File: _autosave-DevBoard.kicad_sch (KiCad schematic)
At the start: 135 parts, among them J1 Audio_In, J10 Jumper, J11 RJ45, J12 Jumper, J13 Jumper, J14 Jumper, J15 Jumper, J16 Jumper, J17 Jumper, J18 DAC_I2S, J19 DAC_OUT, J2 Audio_In, J20 DAC_Amplified, J21 DAC_Amplified, J22 Voltmeter_Power, J23 Voltmeter_Positive, J24 Voltmeter_Ground, J25 Conn_01x05_Pin, J26 Pot1, J27 Pot2, J28 Pot3, J29 Pot4, J3 Audio_Amplified, J30 CV_Scaled_Out1, J31 Audio12V_In, J32 Audio_Scaled_Out, J33 CV_In2, J34 Power, J35 Power, J36 Power, J37 Power, J38 Power, J39 Power_Test, J4 Audio_Amplified, J40 Power, J41 Power_Test, J42 Power, J43 Power, J44 Pot1, J45 Pot2, J46 Pot3, J47 Pot4, J48 CV_In1, J49 CV_Scaled_Out2, J5 CV_In, J50 Audio12V_In, J51 Audio_Scaled_Out, J6 CV_In, J7 CV_Amplified, J8 CV_Amplified, J9 Jumper, SW2 SW_DPDT_x2, U1 MCP6004, U2 TL074, U3 LM1117-3.3, U4 LM1117-5.0, U5 LM4040DBZ-5, U6 PCM5100APW, U8 TL072

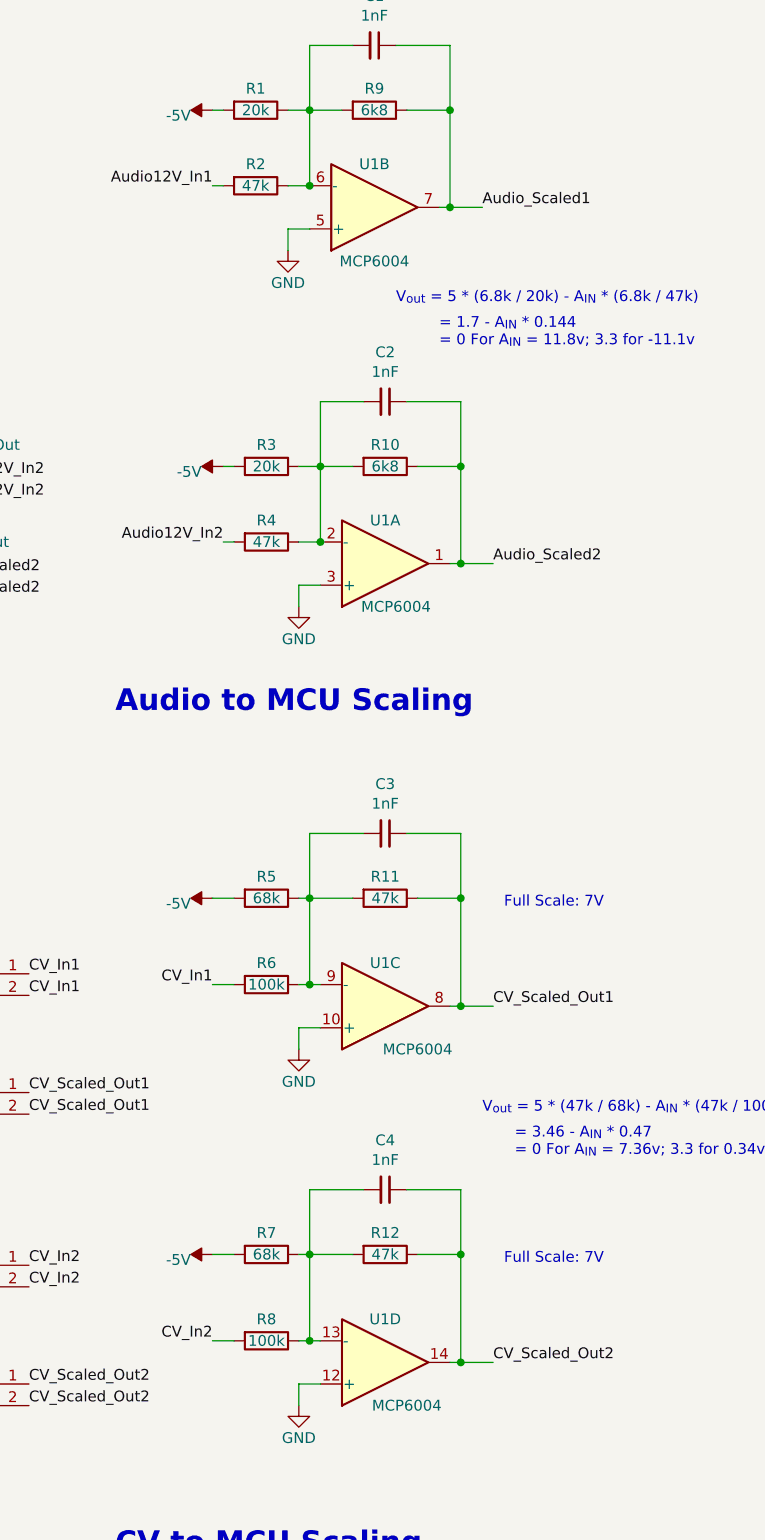
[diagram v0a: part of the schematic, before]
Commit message: Routing scaling circuits
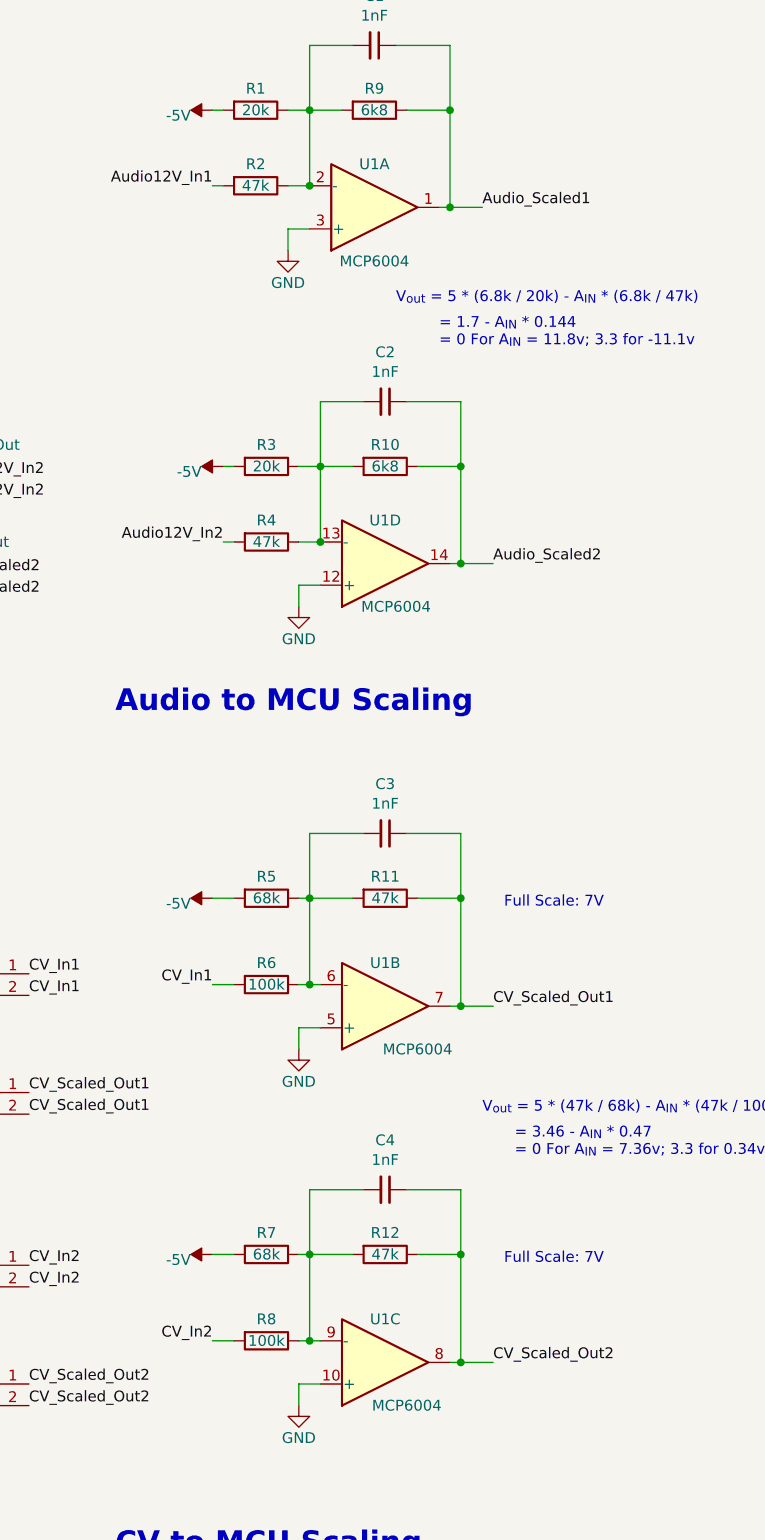
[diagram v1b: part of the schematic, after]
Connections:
- net Audio_Scaled1: now also U1.1; no longer U1.7
- net Audio_Scaled2: now also U1.14; no longer U1.1
- net CV_Scaled_Out1: now also U1.7; no longer U1.8
- net CV_Scaled_Out2: now also U1.8; no longer U1.14
- net GND: now also U1.10 (+), U1.12 (+), U1.3 (+), U1.5 (+); no longer U1.10 (+), U1.12 (+), U1.3 (+), U1.5 (+)
- net at C4.2, R12.2, R7.1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: now also U1.9 (-); no longer U1.13 (-)
- net at C2.2, R10.2, R3.1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: now also U1.13 (-); no longer U1.2 (-)
- net at C3.2, R11.2, R5.1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: now also U1.6 (-); no longer U1.9 (-)
- net at C1.2, R1.1, R2.1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: now also U1.2 (-); no longer U1.6 (-)
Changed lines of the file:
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@@
     )
   )
-  (symbol (lib_id "Amplifier_Operational:MCP6004") (at -52.07 181.61 0) (mirror x) (unit 4)
+  (symbol (lib_id "Amplifier_Operational:MCP6004") (at -52.07 181.61 0) (mirror x) (unit 3)
     (in_bom yes) (on_board yes) (dnp no)
     (property "Reference" "U1" (at -52.07 176.53 0)
@@
       (project "DevBoard"
         (path "/cf927a28-c7bc-4509-acea-70dea4ea1f8a"
-          (reference "U1") (unit 4)
+          (reference "U1") (unit 3)
         )
       )
@@
     )
   )
-  (symbol (lib_id "Amplifier_Operational:MCP6004") (at -52.07 87.63 0) (mirror x) (unit 1)
+  (symbol (lib_id "Amplifier_Operational:MCP6004") (at -52.07 87.63 0) (mirror x) (unit 4)
     (in_bom yes) (on_board yes) (dnp no)
     (property "Reference" "U1" (at -52.07 82.55 0)
@@
       (project "DevBoard"
         (path "/cf927a28-c7bc-4509-acea-70dea4ea1f8a"
-          (reference "U1") (unit 1)
+          (reference "U1") (unit 4)
         )
       )
@@
     )
   )
-  (symbol (lib_id "Amplifier_Operational:MCP6004") (at -52.07 139.7 0) (mirror x) (unit 3)
+  (symbol (lib_id "Amplifier_Operational:MCP6004") (at -52.07 139.7 0) (mirror x) (unit 2)
     (in_bom yes) (on_board yes) (dnp no)
     (property "Reference" "U1" (at -52.07 134.62 0)
@@
       (project "DevBoard"
         (path "/cf927a28-c7bc-4509-acea-70dea4ea1f8a"
-          (reference "U1") (unit 3)
+          (reference "U1") (unit 2)
         )
       )
@@
     )
   )
-  (symbol (lib_id "Amplifier_Operational:MCP6004") (at -53.34 45.72 0) (mirror x) (unit 2)
+  (symbol (lib_id "Amplifier_Operational:MCP6004") (at -53.34 45.72 0) (mirror x) (unit 1)
     (in_bom yes) (on_board yes) (dnp no)
     (property "Reference" "U1" (at -53.34 40.64 0)
@@
       (project "DevBoard"
         (path "/cf927a28-c7bc-4509-acea-70dea4ea1f8a"
-          (reference "U1") (unit 2)
+          (reference "U1") (unit 1)
         )
       )

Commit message: Further layout
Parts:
- removed C10: 1uF, Capacitor_SMD:C_0805_2012Metric, symbol Device:C_Small
- added D3: 5V_LED, LED_SMD:LED_0603_1608Metric, symbol Device:LED_Small
- added D4: 3V3_LED, LED_SMD:LED_0603_1608Metric, symbol Device:LED_Small
- added R36, R37: 2k2, Resistor_SMD:R_0805_2012Metric, symbol Device:R_Small
- D1: value LED_Small -> 12V_LED
- D2: value LED_Small -> -12V_LED
- J6: value CV_In -> CV_Out
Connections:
- net +12V: no longer C9.2, U1.4 (V+)
- net +3.3VA: now also C9.2, U1.4 (V+)
- net +3V3: now also R37.1
- net +5V: now also R36.1
- net -12V: no longer U1.11 (V-)
- net Audio_In1: now also J1.2 (Pin_2); no longer J2.1 (Pin_1)
- net Audio_In2: now also J3.2 (Pin_2); no longer J4.1 (Pin_1)
- net Audio_Out1: now also J2.1 (Pin_1); no longer J1.2 (Pin_2)
- net Audio_Out2: now also J4.1 (Pin_1); no longer J3.2 (Pin_2)
- net CV1_In: now also J5.2 (Pin_2); no longer J6.1 (Pin_1)
- net CV1_Out: now also J6.1 (Pin_1); no longer J5.2 (Pin_2)
- net CV2_In: now also J7.2 (Pin_2); no longer J8.1 (Pin_1)
- net CV2_Out: now also J8.1 (Pin_1); no longer J7.2 (Pin_2)
- net DAC_OUT_AMP_L: now also J20.2 (Pin_2); no longer J21.1 (Pin_1)
- net DAC_OUT_AMP_R: now also J21.1 (Pin_1); no longer J20.2 (Pin_2)
- net GND: now also U1.11 (V-), D3.1 (K), D4.1 (K)
- new net: D4.2 (A), R37.2
- new net: D3.2 (A), R36.2
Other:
- moved on the sheet: D1, R27
